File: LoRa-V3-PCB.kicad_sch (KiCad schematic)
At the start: 88 parts, among them IC1 114993121, IC10 BR24G1MFVT-5AE2, IC11 BR24G1MFVT-5AE2, IC13 MCP73123T-22SI/MF, IC2 CP2102N-Axx-xQFN24, IC3 USBLC6-2P6, IC4 BQ25504RGTR, IC5 BME680, IC6 SHT40-BD1B-R2, IC7 TSL25911FN, IC8 BR24G1MFVT-5AE2, IC9 BR24G1MFVT-5AE2, Q1 PJC7400_R1_00001, Q2 Si2367DS, Q3 Si2367DS, Q4 Si2367DS, SW1 434331045822, SW2 SLLB510100

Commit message: fix JP2 metadata
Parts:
- JP2: manufacturerName (none) -> NA; manufacturerPartNumber (none) -> NA; octopartUrl (none) -> NA
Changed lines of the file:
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@@
+			)
+		)
+		(property "manufacturerName" "NA"
+			(at 189.23 298.45 0)
+			(effects
+				(font
+					(size 1.27 1.27)
+				)
+				(hide yes)
+			)
+		)
+		(property "manufacturerPartNumber" "NA"
+			(at 189.23 298.45 0)
+			(effects
+				(font
+					(size 1.27 1.27)
+				)
+				(hide yes)
+			)
+		)
+		(property "octopartUrl" "NA"
+			(at 189.23 298.45 0)
+			(effects
+				(font
+					(size 1.27 1.27)
+				)
+				(hide yes)
 			)
 		)

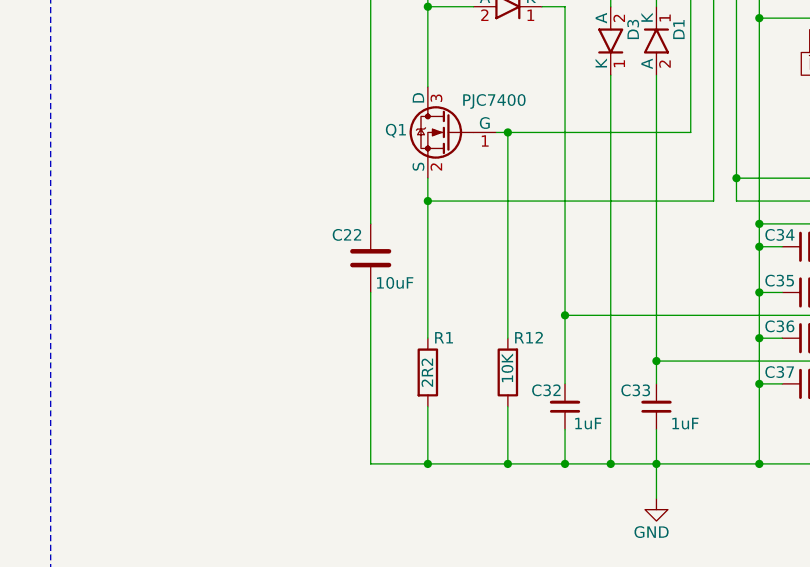
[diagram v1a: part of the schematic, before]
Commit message: add extra csv file for kicost
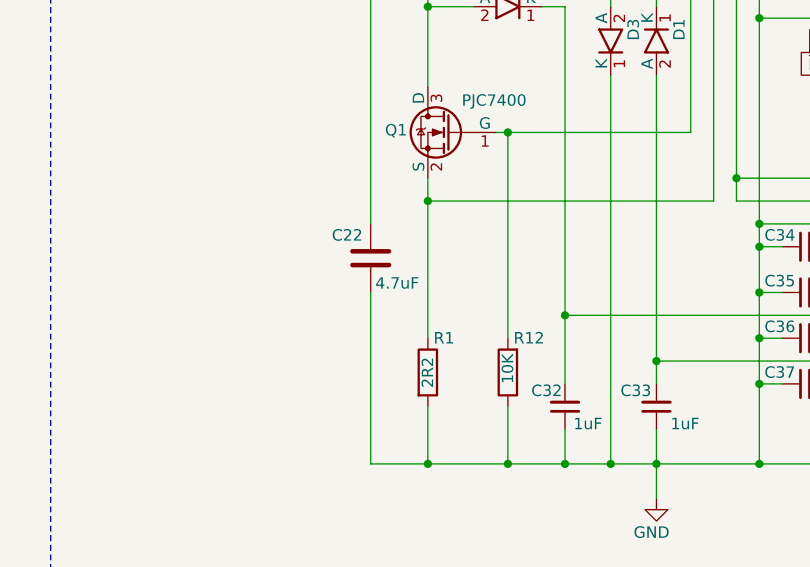
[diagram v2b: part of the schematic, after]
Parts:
- C22: value 10uF -> 4.7uF; manufacturerPartNumber CL21B106KPQNNWE -> CL21B475KPFNFNE; octopartUrl https://octopart.com/cl21b106kpqnnwe-samsung+electro-mechan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 -> https://octopart.com/cl21b475kpfnfne-samsung+electro-mechan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
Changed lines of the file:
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@@
 			)
 		)
-		(property "Value" "10uF"
+		(property "Value" "4.7uF"
 			(at 481.838 131.064 0)
 			(effects
@@
 			)
 		)
-		(property "Datasheet" "https://octopart.com/datasheet/cl21b106kpqnnwe-samsung+electro-mechanics-52884428"
+		(property "Datasheet" "https://octopart.com/datasheet/cl21b475kpfnfne-samsung+electro-mechanics-24958210"
 			(at 481.33 128.27 0)
 			(effects
@@
 			)
 		)
-		(property "octopartUrl" "https://octopart.com/cl21b106kpqnnwe-samsung+electro-mechanics-52884428"
+		(property "octopartUrl" "https://octopart.com/cl21b475kpfnfne-samsung+electro-mechanics-24958210"
 			(at 481.33 128.27 0)
 			(effects
@@
 			)
 		)
-		(property "manufacturerPartNumber" "CL21B106KPQNNWE"
+		(property "manufacturerPartNumber" "CL21B475KPFNFNE"
 			(at 481.33 128.27 0)
 			(effects

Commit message: remove connectors from BOM
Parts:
- CONN4, CONN8: now left out of the parts list
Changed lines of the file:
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@@
 		(unit 1)
 		(exclude_from_sim no)
-		(in_bom yes)
+		(in_bom no)
 		(on_board yes)
 		(dnp no)
@@
 		(unit 1)
 		(exclude_from_sim no)
-		(in_bom yes)
+		(in_bom no)
 		(on_board yes)
 		(dnp no)

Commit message: add silkscreen logo version and date
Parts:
- IC1: manufacturerPartNumber 114993121 -> 317990687; mouserPartNumber (none) -> 713-317990687
- renumbered C17 to C10, C20 to C17, C22 to C18, C10 to C26, C18 to C27, CONN7 to CONN3, IC13 to IC12
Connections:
- net TEST0: now reaches IC1.28 (PB0)
- no-connect marks 24 -> 23
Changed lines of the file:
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@@
 	)
 	(no_connect
-		(at 386.08 91.44)
-	)
-	(no_connect
 		(at 350.52 93.98)
 	)
@@
 	(wire
 		(pts
+			(xy 386.08 91.44) (xy 394.97 91.44)
+		)
+		(stroke
+			(width 0)
+			(type default)
+		)
+	)
+	(wire
+		(pts
 			(xy 375.92 69.85) (xy 388.62 69.85)
 		)
@@
 		)
 	)
+	(global_label "TEST0"
+		(shape input)
+		(at 394.97 91.44 0)
+		(fields_autoplaced yes)
+		(effects
+			(font
+				(size 1.27 1.27)
+			)
+			(justify left)
+		)
+		(property "Intersheetrefs" "${INTERSHEET_REFS}"
+			(at 403.4584 91.44 0)
+			(effects
+				(font
+					(size 1.27 1.27)
+				)
+				(justify left)
+				(hide yes)
+			)
+		)
+	)
 	(global_label "Solar+"
 		(shape input)
@@
 			)
 		)
-		(property "manufacturerPartNumber" "114993121"
+		(property "manufacturerPartNumber" "317990687"
 			(at 323.088 99.822 0)
 			(effects
@@
 			)
 		)
+		(property "mouserPartNumber" "713-317990687"
+			(at 331.216 99.06 0)
+			(effects
+				(font
+					(size 1.27 1.27)
+				)
+				(hide yes)
+			)
+		)
+		(property "OctoPartURL" ""
+			(at 368.3 99.06 0)
+			(effects
+				(font
+					(size 1.27 1.27)
+				)
+				(hide yes)
+			)
+		)
 		(pin "1"
 		)
@@
 		(on_board yes)
 		(dnp no)
-		(property "Reference" "IC13"
+		(property "Reference" "IC12"
 			(at 194.31 109.22 0)
 			(effects
@@
 			(project "LoRa-V3-PCB"
 				(path "/8b98a678-96e2-411a-8566-924f77e9f267"
-					(reference "IC13")
+					(reference "IC12")
 					(unit 1)
 				)
@@
 		(on_board yes)
 		(dnp no)
-		(property "Reference" "CONN7"
+		(property "Reference" "CONN3"
 			(at 144.272 372.11 0)
 			(effects
@@
 			(project "LoRa-V3-PCB"
 				(path "/8b98a678-96e2-411a-8566-924f77e9f267"
-					(reference "CONN7")
+					(reference "CONN3")
 					(unit 1)
 				)
@@
 		(on_board yes)
 		(dnp no)
-		(property "Reference" "C10"
+		(property "Reference" "C26"
 			(at 393.192 72.39 0)
 			(effects
@@
 			(project "LoRa-V3-PCB"
 				(path "/8b98a678-96e2-411a-8566-924f77e9f267"
-					(reference "C10")
+					(reference "C26")
 					(unit 1)
 				)
@@
 		(on_board yes)
 		(dnp no)
-		(property "Reference" "C22"
+		(property "Reference" "C18"
 			(at 477.012 125.73 0)
 			(effects
@@
 			(project "LoRa-V3-PCB"
 				(path "/8b98a678-96e2-411a-8566-924f77e9f267"
-					(reference "C22")
+					(reference "C18")
 					(unit 1)
 				)
@@
 		(on_board yes)
 		(dnp no)
-		(property "Reference" "C20"
+		(property "Reference" "C17"
 			(at 58.928 105.156 0)
 			(effects
@@
 			(project "LoRa-V3-PCB"
 				(path "/8b98a678-96e2-411a-8566-924f77e9f267"
-					(reference "C20")
+					(reference "C17")
 					(unit 1)
 				)
@@
 		(on_board yes)
 		(dnp no)
-		(property "Reference" "C17"
+		(property "Reference" "C10"
 			(at 141.732 97.536 0)
 			(effects
@@
 			(project "LoRa-V3-PCB"
 				(path "/8b98a678-96e2-411a-8566-924f77e9f267"
-					(reference "C17")
+					(reference "C10")
 					(unit 1)
 				)
@@
 		(on_board yes)
 		(dnp no)
-		(property "Reference" "C18"
+		(property "Reference" "C27"
 			(at 518.922 59.69 0)
 			(effects
@@
 			(project "LoRa-V3-PCB"
 				(path "/8b98a678-96e2-411a-8566-924f77e9f267"
-					(reference "C18")
+					(reference "C27")
 					(unit 1)
 				)

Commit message: fix BOM
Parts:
- IC1: OctoPartURL (none) -> https://octopart.com/search?q=317990687&currency=USD&specs=0
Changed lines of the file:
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@@
 			)
 		)
-		(property "OctoPartURL" ""
+		(property "OctoPartURL" "https://octopart.com/search?q=317990687&currency=USD&specs=0"
 			(at 368.3 99.06 0)
 			(effects

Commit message: fix BOM 2
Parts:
- IC1: value 114993121 -> SeeedStudio Wio-E5-LE-HF; OctoPartURL https://octopart.com/search?q=317990687&currency=USD&specs=0 -> (none); manufacturerPartNumber 317990687 -> 114993121; mouserPartNumber 713-317990687 -> (none); octopartUrl https://octopart.com/114993121-seeed+studio-142683940?r=sp -> https://octopart.com/114993121-seeed+studio-142683940
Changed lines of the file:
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@@
 			)
 		)
-		(property "Value" "114993121"
+		(property "Value" "SeeedStudio Wio-E5-LE-HF"
 			(at 368.427 99.187 90)
 			(effects
@@
 			)
 		)
-		(property "octopartUrl" "https://octopart.com/114993121-seeed+studio-142683940?r=sp"
+		(property "octopartUrl" "https://octopart.com/114993121-seeed+studio-142683940"
 			(at 368.3 99.06 0)
 			(effects
@@
 			)
 		)
-		(property "manufacturerPartNumber" "317990687"
+		(property "manufacturerPartNumber" "114993121"
 			(at 323.088 99.822 0)
 			(effects
 				(font
-					(size 1.27 1.27)
-				)
-				(hide yes)
-			)
-		)
-		(property "mouserPartNumber" "713-317990687"
-			(at 331.216 99.06 0)
-			(effects
-				(font
-					(size 1.27 1.27)
-				)
-				(hide yes)
-			)
-		)
-		(property "OctoPartURL" "https://octopart.com/search?q=317990687&currency=USD&specs=0"
-			(at 368.3 99.06 0)
-			(effects
-				(font

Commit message: replace 5M36 resistor
by a variant which is in stock
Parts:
- R11, R21: manufacturerName YAGEO -> Vishay - Dale; manufacturerPartNumber RC0603FR-075M36L -> CRCW06035M36FKEA; octopartUrl https://octopart.com/rc0603fr-075m36l-yageo-24734316 -> https://octopart.com/crcw06035m36fkea-vishay-39816157

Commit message: fix BOM
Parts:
- D1, D2, D3: symbol 1projectLibrary:SDM05U40CSP-7 -> 1projectLibrary:D
- L1: symbol 1projectLibrary:VLS3010CX-470M-1 -> Device:L
